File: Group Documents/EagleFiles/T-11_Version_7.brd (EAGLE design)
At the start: 79.7 x 74.9 mm, 52 parts, among them SW1 SW-1801X, SW2 SW-1801X, U1 ATMEGA328P-AU, X1 SMA-142-0701-871/880

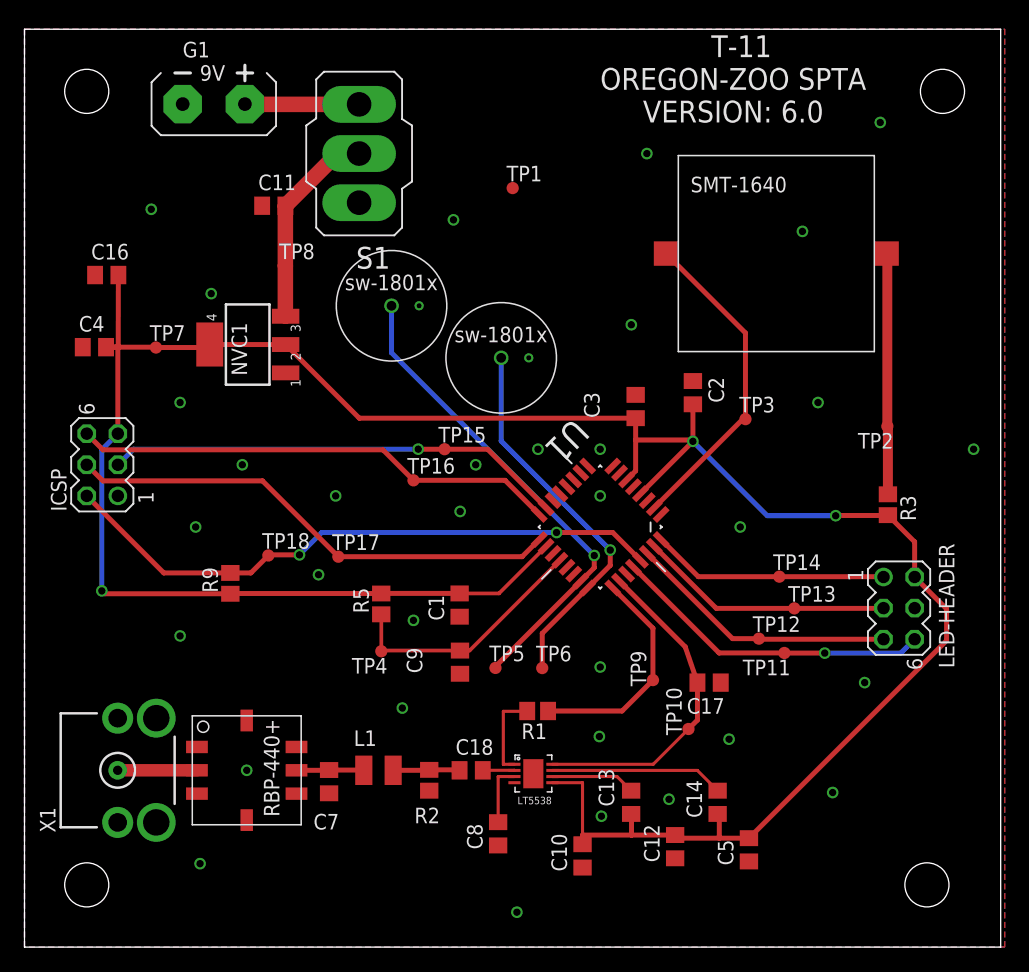
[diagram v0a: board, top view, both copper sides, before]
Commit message: layout 7
updated schematic.
updated SPTA layout.
updated LED brake-out layout.
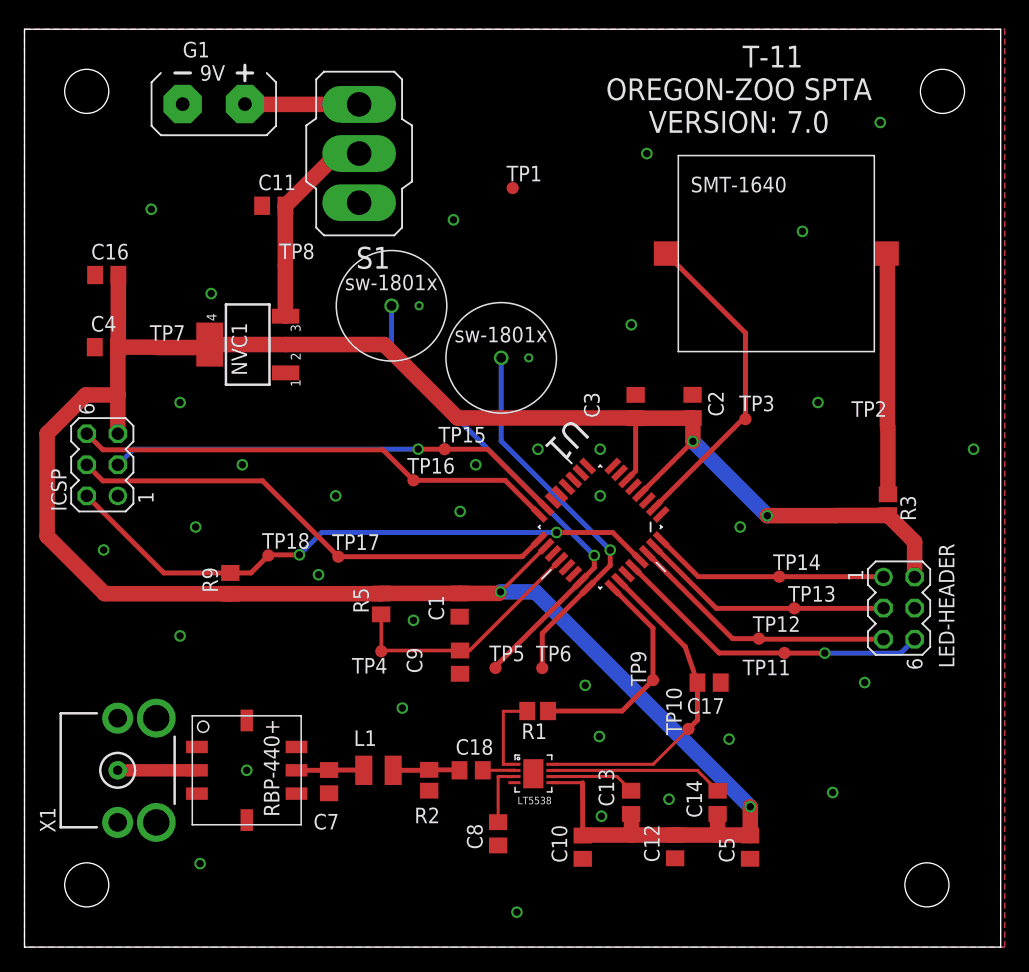
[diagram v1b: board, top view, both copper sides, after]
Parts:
- R5: value 20k -> DNC
- moved C2 1.13 mm to (54.5, 44.1)
- moved C4 0.98 mm to (6.69, 49.0)
- moved C10 0.71 mm to (45.6, 8.15)
- moved C5 0.24 mm to (59.2, 8.16)
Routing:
- net +5V: track 210.6 -> 214.4 mm, vias 3 -> 4
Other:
- board text added: "T-11 OREGON-ZOO SPTA VERSION: 7.0"
- board text removed: "T-11 OREGON-ZOO SPTA VERSION: 6.0"
